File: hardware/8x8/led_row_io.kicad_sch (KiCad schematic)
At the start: 12 parts

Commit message: Updated LED Driver Footprints
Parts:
- LED_Driver_1: footprint LED Driver:PCA9956BTWY -> LED Driver:SOP50P640X110-39N
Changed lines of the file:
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@@
       (effects (font (size 1.27 1.27)) hide)
     )
-    (property "Footprint" "LED Driver:PCA9956BTWY" (id 2) (at 218.44 83.82 0)
+    (property "Footprint" "LED Driver:SOP50P640X110-39N" (id 2) (at 218.44 83.82 0)
       (effects (font (size 1.27 1.27)) (justify left bottom) hide)
     )

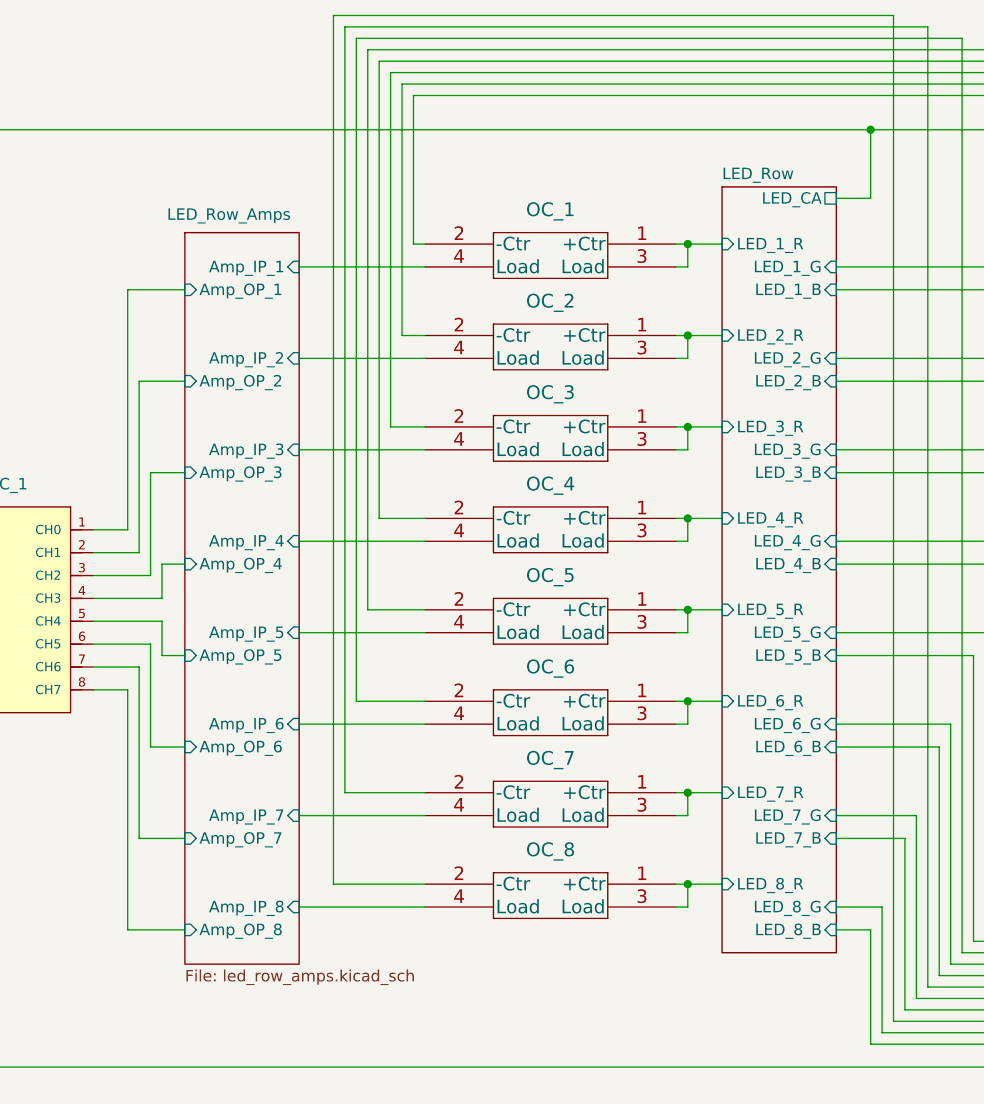
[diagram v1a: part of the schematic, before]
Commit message: Temporary Component Placement on PCB
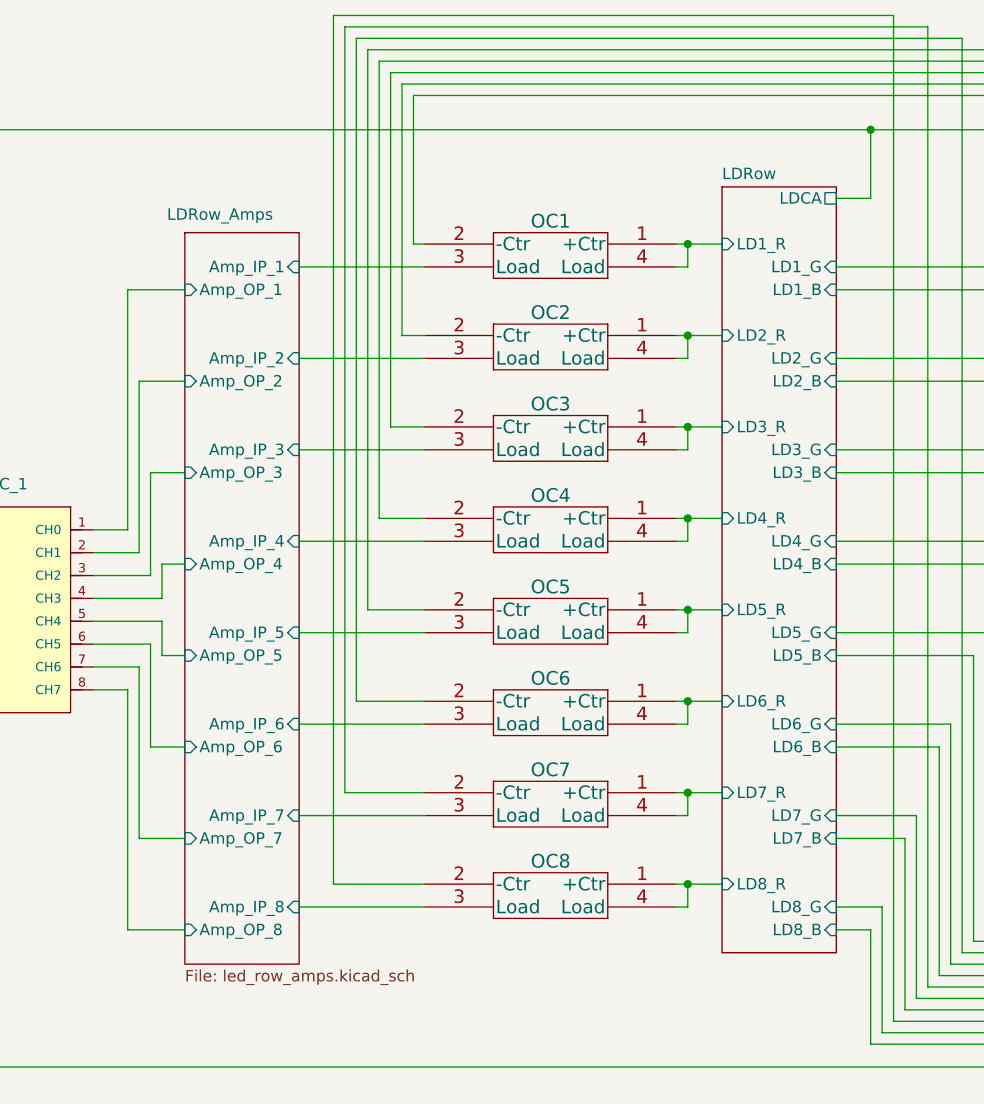
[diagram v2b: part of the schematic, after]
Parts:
- removed OC_2, OC_3, OC_4, OC_5, OC_6, OC_7, OC_8: CPC1125N, Opto-coupler:footprints, symbol Opto-coupler:CPC1125N
- added OC2, OC3, OC4, OC5, OC6, OC7, OC8: CPC1125N, Opto-coupler:footprints, symbol Opto-coupler:CPC1125N
- renumbered OC_1 to OC1
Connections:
- net  LDRow_Amps/Amp_IP_1: now also OC1.3 (Load); no longer OC1.4 (Load)
- net  LDRow_Amps/Amp_IP_2: now also OC2.3 (Load)
- net  LDRow_Amps/Amp_IP_3: now also OC3.3 (Load)
- net  LDRow_Amps/Amp_IP_4: now also OC4.3 (Load)
- net  LDRow_Amps/Amp_IP_5: now also OC5.3 (Load)
- net  LDRow_Amps/Amp_IP_6: now also OC6.3 (Load)
- net  LDRow_Amps/Amp_IP_7: now also OC7.3 (Load)
- net  LDRow_Amps/Amp_IP_8: now also OC8.3 (Load)
- net at LED_Driver_1.31 (LED21): now also OC8.2 (-Ctr)
- net at LED_Driver_1.12 (LED6): now also OC3.2 (-Ctr)
- net at LED_Driver_1.16 (LED9): now also OC4.2 (-Ctr)
- net at LED_Driver_1.20 (LED12): now also OC5.2 (-Ctr)
- net at LED_Driver_1.24 (LED15): now also OC6.2 (-Ctr)
- net at LED_Driver_1.28 (LED18): now also OC7.2 (-Ctr)
- net at LED_Driver_1.9 (LED3): now also OC2.2 (-Ctr)
- net LDRow/LED_1_B renamed LDRow/LD1_B
- net LDRow/LED_1_G renamed LDRow/LD1_G
- net LDRow/LED_1_R renamed LDRow/LD1_R
- net LDRow/LD1_R: now also OC1.4 (Load); no longer OC1.3 (Load)
- net LDRow/LED_2_B renamed LDRow/LD2_B
- net LDRow/LED_2_G renamed LDRow/LD2_G
- net LDRow/LED_3_B renamed LDRow/LD3_B
- net LDRow/LED_3_G renamed LDRow/LD3_G
- net LDRow/LED_4_B renamed LDRow/LD4_B
- net LDRow/LED_4_G renamed LDRow/LD4_G
- net LDRow/LED_5_B renamed LDRow/LD5_B
- net LDRow/LED_5_G renamed LDRow/LD5_G
- net LDRow/LED_6_B renamed LDRow/LD6_B
- net LDRow/LED_6_G renamed LDRow/LD6_G
- net LDRow/LED_7_B renamed LDRow/LD7_B
- net LDRow/LED_7_G renamed LDRow/LD7_G
- net LDRow/LED_8_B renamed LDRow/LD8_B
- net LDRow/LED_8_G renamed LDRow/LD8_G
- new net LDRow/LD2_R: OC2.1 (+Ctr), OC2.4 (Load)
- new net LDRow/LD3_R: OC3.1 (+Ctr), OC3.4 (Load)
- new net LDRow/LD4_R: OC4.1 (+Ctr), OC4.4 (Load)
- new net LDRow/LD5_R: OC5.1 (+Ctr), OC5.4 (Load)
- new net LDRow/LD6_R: OC6.1 (+Ctr), OC6.4 (Load)
- new net LDRow/LD7_R: OC7.1 (+Ctr), OC7.4 (Load)
- new net LDRow/LD8_R: OC8.1 (+Ctr), OC8.4 (Load)
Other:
- sheet  LED_Row_Amps renamed  LDRow_Amps
- sheet LED_Row renamed LDRow
- sheet LDRow ports: added LD1_B, LD1_G, LD1_R, LD2_B, LD2_G, LD2_R, LD3_B, LD3_G, LD3_R, LD4_B, LD4_G, LD4_R, LD5_B, LD5_G, LD5_R, LD6_B, LD6_G, LD6_R, LD7_B, LD7_G, LD7_R, LD8_B, LD8_G, LD8_R, LDCA; removed LED_1_B, LED_1_G, LED_1_R, LED_2_B, LED_2_G, LED_2_R, LED_3_B, LED_3_G, LED_3_R, LED_4_B, LED_4_G, LED_4_R, LED_5_B, LED_5_G, LED_5_R, LED_6_B, LED_6_G, LED_6_R, LED_7_B, LED_7_G, LED_7_R, LED_8_B, LED_8_G, LED_8_R, LED_CA

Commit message: Updated Components
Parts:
- SSR1: renamed from OC1; value CPC1125N -> TLP4176ATP_F; footprint Opto-coupler:footprints -> SSR:footprints; symbol Opto-coupler:CPC1125N -> SSR:TLP4176ATP_F
- SSR2: renamed from OC2; value CPC1125N -> TLP4176ATP_F; footprint Opto-coupler:footprints -> SSR:footprints; symbol Opto-coupler:CPC1125N -> SSR:TLP4176ATP_F
- SSR3: renamed from OC3; value CPC1125N -> TLP4176ATP_F; footprint Opto-coupler:footprints -> SSR:footprints; symbol Opto-coupler:CPC1125N -> SSR:TLP4176ATP_F
- SSR4: renamed from OC4; value CPC1125N -> TLP4176ATP_F; footprint Opto-coupler:footprints -> SSR:footprints; symbol Opto-coupler:CPC1125N -> SSR:TLP4176ATP_F
- SSR5: renamed from OC5; value CPC1125N -> TLP4176ATP_F; footprint Opto-coupler:footprints -> SSR:footprints; symbol Opto-coupler:CPC1125N -> SSR:TLP4176ATP_F
- SSR6: renamed from OC6; value CPC1125N -> TLP4176ATP_F; footprint Opto-coupler:footprints -> SSR:footprints; symbol Opto-coupler:CPC1125N -> SSR:TLP4176ATP_F
- SSR7: renamed from OC7; value CPC1125N -> TLP4176ATP_F; footprint Opto-coupler:footprints -> SSR:footprints; symbol Opto-coupler:CPC1125N -> SSR:TLP4176ATP_F
- SSR8: renamed from OC8; value CPC1125N -> TLP4176ATP_F; footprint Opto-coupler:footprints -> SSR:footprints; symbol Opto-coupler:CPC1125N -> SSR:TLP4176ATP_F

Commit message: Updated Footprints
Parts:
- ISEL1: renamed from Drv_I_Sel_1; footprint Resistor_THT:R_Axial_DIN0207_L6.3mm_D2.5mm_P7.62mm_Horizontal -> Resistor TH:footprints
- PU1: renamed from Drv_RST_PU_1; footprint Resistor_THT:R_Axial_DIN0207_L6.3mm_D2.5mm_P7.62mm_Horizontal -> Resistor TH:footprints
- renumbered ADC_1 to AD1, LED_Driver_1 to DRV1, SSR1 to SR1, SSR2 to SR2, SSR3 to SR3, SSR4 to SR4, SSR5 to SR5, SSR6 to SR6, SSR7 to SR7, SSR8 to SR8
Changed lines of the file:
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@@
   (symbol (lib_id "SSR:TLP4176ATP_F") (at 106.68 87.63 0) (unit 1)
     (in_bom yes) (on_board yes)
-    (property "Reference" "SSR5" (id 0) (at 106.68 83.82 0)
+    (property "Reference" "SR5" (id 0) (at 106.68 83.82 0)
       (effects (font (size 1.524 1.524)))
     )
@@
   (symbol (lib_id "SSR:TLP4176ATP_F") (at 106.68 118.11 0) (unit 1)
     (in_bom yes) (on_board yes)
-    (property "Reference" "SSR8" (id 0) (at 106.68 114.3 0)
+    (property "Reference" "SR8" (id 0) (at 106.68 114.3 0)
       (effects (font (size 1.524 1.524)))
     )
@@
   (symbol (lib_id "ADC:MCU-MCP3008-I{brace}slash}P(DIP16-7.62MM)") (at 45.72 86.36 0) (mirror y) (unit 1)
     (in_bom yes) (on_board yes)
-    (property "Reference" "ADC_1" (id 0) (at 45.72 72.39 0))
+    (property "Reference" "AD1" (id 0) (at 45.72 72.39 0))
     (property "Value" "MCU-MCP3008-I/P(DIP16-7.62MM)" (id 1) (at 46.101 73.66 0)
       (effects (font (size 1.27 1.27)) hide)
@@
   (symbol (lib_id "SSR:TLP4176ATP_F") (at 106.68 97.79 0) (unit 1)
     (in_bom yes) (on_board yes)
-    (property "Reference" "SSR6" (id 0) (at 106.68 93.98 0)
+    (property "Reference" "SR6" (id 0) (at 106.68 93.98 0)
       (effects (font (size 1.524 1.524)))
     )
@@
   (symbol (lib_id "SSR:TLP4176ATP_F") (at 106.68 57.15 0) (unit 1)
     (in_bom yes) (on_board yes)
-    (property "Reference" "SSR2" (id 0) (at 106.68 53.34 0)
+    (property "Reference" "SR2" (id 0) (at 106.68 53.34 0)
       (effects (font (size 1.524 1.524)))
     )
@@
   (symbol (lib_id "Device:R") (at 198.12 66.04 90) (mirror x) (unit 1)
     (in_bom yes) (on_board yes) (fields_autoplaced)
-    (property "Reference" "Drv_I_Sel_1" (id 0) (at 198.12 59.69 90))
+    (property "Reference" "ISEL1" (id 0) (at 198.12 59.69 90))
     (property "Value" "2K" (id 1) (at 198.12 62.23 90))
-    (property "Footprint" "Resistor_THT:R_Axial_DIN0207_L6.3mm_D2.5mm_P7.62mm_Horizontal" (id 2) (at 198.12 64.262 90)
+    (property "Footprint" "Resistor TH:footprints" (id 2) (at 198.12 64.262 90)
       (effects (font (size 1.27 1.27)) hide)
     )
@@
   (symbol (lib_id "LED Driver:PCA9956BTWY") (at 218.44 83.82 0) (unit 1)
     (in_bom yes) (on_board yes) (fields_autoplaced)
-    (property "Reference" "LED_Driver_1" (id 0) (at 218.44 53.34 0))
+    (property "Reference" "DRV1" (id 0) (at 218.44 53.34 0))
     (property "Value" "PCA9956BTWY" (id 1) (at 218.44 53.34 0)
       (effects (font (size 1.27 1.27)) hide)
@@
   (symbol (lib_id "SSR:TLP4176ATP_F") (at 106.68 107.95 0) (unit 1)
     (in_bom yes) (on_board yes)
-    (property "Reference" "SSR7" (id 0) (at 106.68 104.14 0)
+    (property "Reference" "SR7" (id 0) (at 106.68 104.14 0)
       (effects (font (size 1.524 1.524)))
     )
@@
   (symbol (lib_id "SSR:TLP4176ATP_F") (at 106.68 67.31 0) (unit 1)
     (in_bom yes) (on_board yes)
-    (property "Reference" "SSR3" (id 0) (at 106.68 63.5 0)
+    (property "Reference" "SR3" (id 0) (at 106.68 63.5 0)
       (effects (font (size 1.524 1.524)))
     )
@@
   (symbol (lib_id "SSR:TLP4176ATP_F") (at 106.68 77.47 0) (unit 1)
     (in_bom yes) (on_board yes)
-    (property "Reference" "SSR4" (id 0) (at 106.68 73.66 0)
+    (property "Reference" "SR4" (id 0) (at 106.68 73.66 0)
       (effects (font (size 1.524 1.524)))
     )
@@
   (symbol (lib_id "Device:R") (at 204.47 48.26 0) (unit 1)
     (in_bom yes) (on_board yes) (fields_autoplaced)
-    (property "Reference" "Drv_RST_PU_1" (id 0) (at 207.01 46.9899 0)
+    (property "Reference" "PU1" (id 0) (at 207.01 46.9899 0)
       (effects (font (size 1.27 1.27)) (justify left))
     )
@@
       (effects (font (size 1.27 1.27)) (justify left))
     )
-    (property "Footprint" "Resistor_THT:R_Axial_DIN0207_L6.3mm_D2.5mm_P7.62mm_Horizontal" (id 2) (at 202.692 48.26 90)
+    (property "Footprint" "Resistor TH:footprints" (id 2) (at 202.692 48.26 90)
       (effects (font (size 1.27 1.27)) hide)
     )
@@
   (symbol (lib_id "SSR:TLP4176ATP_F") (at 106.68 46.99 0) (unit 1)
     (in_bom yes) (on_board yes)
-    (property "Reference" "SSR1" (id 0) (at 106.68 43.18 0)
-      (effects (font (size 1.524 1.524)))
-    )
+    (property "Reference" "SR1" (id 0) (at 106.68 43.18 0)
+      (effects (font (size 1.524 1.524)))
+    )
